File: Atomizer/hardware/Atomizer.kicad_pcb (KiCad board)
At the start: 2 copper layers, 54.6 x 98.6 mm, 41 parts

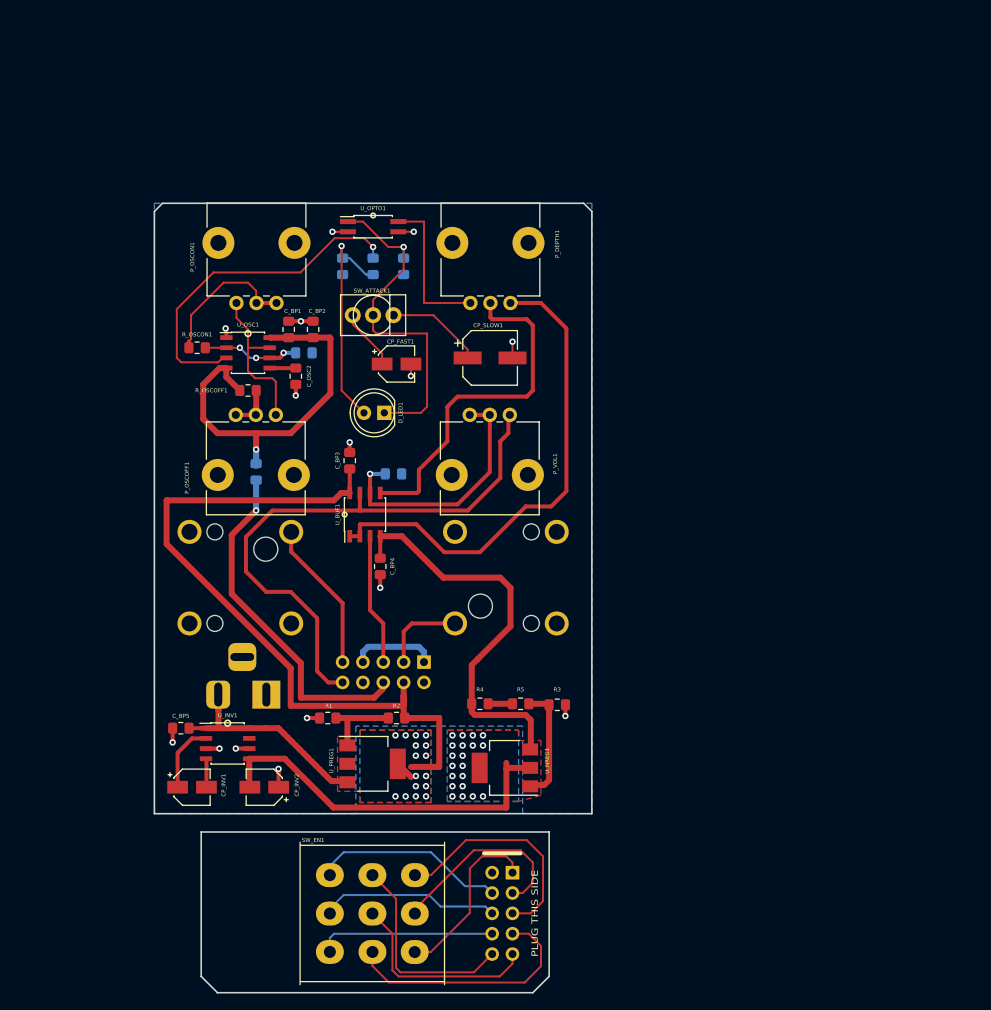
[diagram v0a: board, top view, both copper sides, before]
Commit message: Added 3d Model
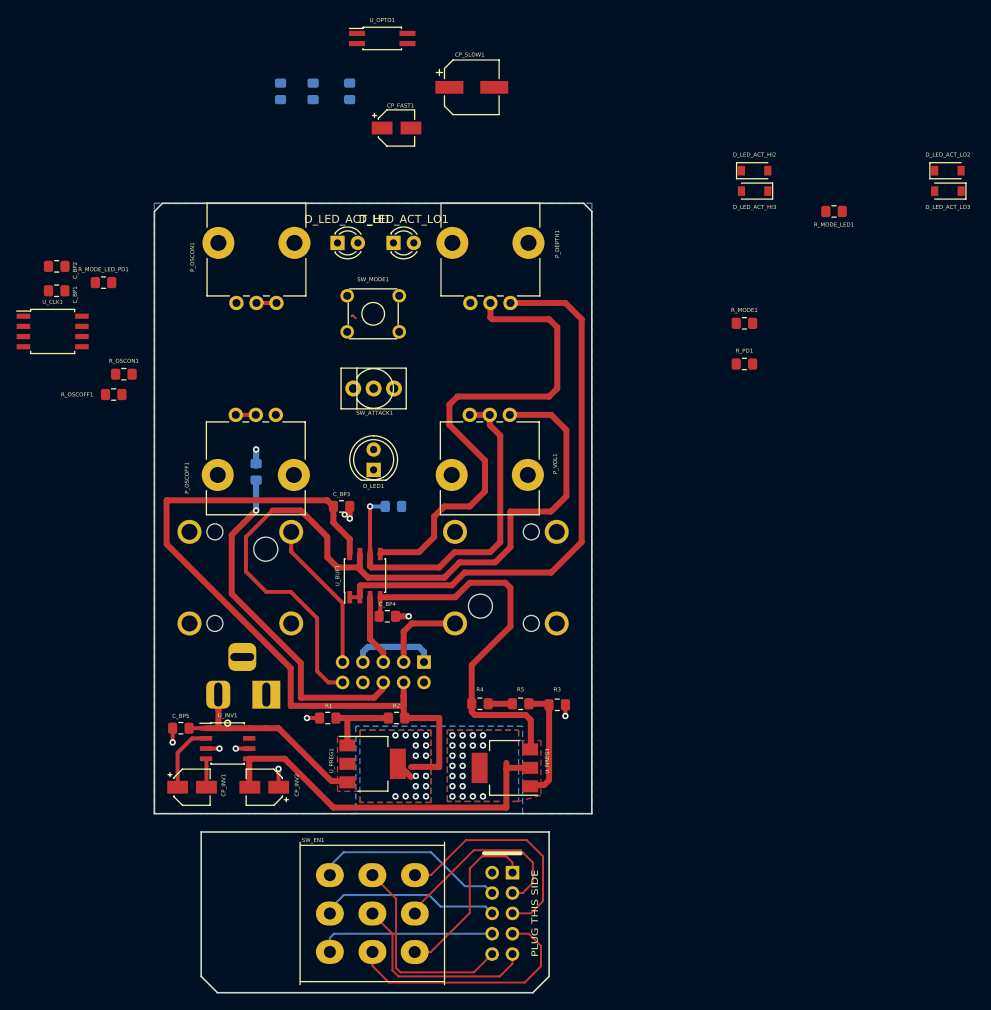
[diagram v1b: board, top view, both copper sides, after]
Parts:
- removed C_OSC1: 22uF, Capacitor_SMD:C_0805_2012Metric_Pad1.15x1.40mm_HandSolder
- removed C_OSC2: 100nF, Capacitor_SMD:C_0805_2012Metric_Pad1.15x1.40mm_HandSolder
- removed U_OSC1: TLC555, Package_SO:SOIC-8_3.9x4.9mm_P1.27mm
- added D_LED_ACT_HI1: LED, LED_THT:LED_D3.0mm, F.Cu at (76.2, 76.3)
- added D_LED_ACT_HI2: 1N914_VF1, Diode_SMD:D_SOD-123, F.Cu at (128.3, 67.3)
- added D_LED_ACT_HI3: 1N914_VF1, Diode_SMD:D_SOD-123, F.Cu at (128.3, 69.8)
- added D_LED_ACT_LO1: LED, LED_THT:LED_D3.0mm, F.Cu at (83.2, 76.3)
- added D_LED_ACT_LO2: 1N914_VF1, Diode_SMD:D_SOD-123, F.Cu at (152.4, 67.3)
- added D_LED_ACT_LO3: 1N914_VF1, Diode_SMD:D_SOD-123, F.Cu at (152.4, 69.8)
- added R_MODE1: 1K, Resistor_SMD:R_0805_2012Metric_Pad1.15x1.40mm_HandSolder, F.Cu at (127.0, 86.4)
- added R_MODE_LED1: 22K, Resistor_SMD:R_0805_2012Metric_Pad1.15x1.40mm_HandSolder, F.Cu at (138.2, 72.4)
- added R_MODE_LED_PD1: 47K, Resistor_SMD:R_0805_2012Metric_Pad1.15x1.40mm_HandSolder, F.Cu at (47.0, 81.3)
- added R_PD1: 22M, Resistor_SMD:R_0805_2012Metric_Pad1.15x1.40mm_HandSolder, F.Cu at (127.0, 91.4)
- added SW_MODE1: SW_SPST, TE_Alcoswitch_Tactile_FSM_RAJ:SW_TH_Tactile_Omron_B3F-10xx, F.Cu at (77.4, 82.9)
- added U_CLK1: ATtiny85-20SU, Package_SO:SOIJ-8_5.3x5.3mm_P1.27mm, F.Cu at (40.6, 87.4)
- C_BP2: value 47uF -> 10uF
- U_OPTO1: value LTV-357T -> ACPL-217
- moved CP_SLOW1 33.9 mm to (93.0, 56.9)
- moved C_BP2 33.0 mm to (41.1, 79.2), turned to 0 degrees
- moved CP_FAST1 29.5 mm to (83.6, 62.0)
- moved C_BP1 29.4 mm to (41.1, 82.3), turned to 0 degrees
- moved C_LPFOPT2 24.6 mm to (73.2, 57.4)
- moved U_OPTO1 23.5 mm to (81.8, 50.8)
- moved C_LPFOPT1 23.2 mm to (69.1, 57.4)
- moved R_LPF1 22.0 mm to (77.7, 57.4)
- moved R_OSCOFF1 16.8 mm to (48.3, 95.2)
- moved R_OSCON1 9.72 mm to (49.5, 92.7)
- moved SW_ATTACK1 9.15 mm to (80.7, 94.5), turned to 90 degrees
- moved U_BUF1 7.62 mm to (79.6, 117.9)
- moved D_LED1 7.24 mm to (80.7, 104.7), turned to 90 degrees
- moved C_BP4 6.29 mm to (82.4, 122.9), turned to 0 degrees
- moved C_BP3 5.80 mm to (76.7, 109.2), turned to 180 degrees
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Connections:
- net /555PWMTremolo_3PDT/3PDT_1_INT renamed /Atomizer_3PDT/3PDT_1_INT
- net /555PWMTremolo_3PDT/3PDT_2_INT renamed /Atomizer_3PDT/3PDT_2_INT
- net /555PWMTremolo_3PDT/3PDT_3_INT renamed /Atomizer_3PDT/3PDT_3_INT
- net /555PWMTremolo_3PDT/3PDT_4_INT renamed /Atomizer_3PDT/3PDT_4_INT
- net /555PWMTremolo_3PDT/3PDT_5_INT renamed /Atomizer_3PDT/3PDT_5_INT
- net /555PWMTremolo_3PDT/3PDT_6_INT renamed /Atomizer_3PDT/3PDT_6_INT
- net /555PWMTremolo_3PDT/3PDT_7_INT renamed /Atomizer_3PDT/3PDT_7_INT
- net /555PWMTremolo_3PDT/3PDT_8_INT renamed /Atomizer_3PDT/3PDT_8_INT
- net /555PWMTremolo_3PDT/3PDT_9_INT renamed /Atomizer_3PDT/3PDT_9_INT
- net /555PWMTremolo_Clock/CLK_OUT renamed /Atomizer_Clock/CLK_OUT
- P_OSCOFF1 pad 1: Net-(P_OSCOFF1-Pad1) -> /GND
- P_OSCOFF1 pad 2: Net-(P_OSCOFF1-Pad1) -> /Atomizer_Clock/FREQ_ADJ_OFF_PIN
- P_OSCON1 pad 1: Net-(P_OSCON1-Pad1) -> /GND
- P_OSCON1 pad 2: Net-(P_OSCON1-Pad1) -> /Atomizer_Clock/FREQ_ADJ_ON_PIN
- P_OSCON1 pad 3: Net-(P_OSCOFF1-Pad3) -> Net-(P_OSCON1-Pad3)
- R_LPF1 pad 2: Net-(R_LPF1-Pad2) -> /Atomizer_Clock/CLK_OUT_PIN
- R_OSCOFF1 pad 1: Net-(P_OSCOFF1-Pad1) -> Net-(P_OSCOFF1-Pad3)
- R_OSCOFF1 pad 2: Net-(C_BP1-Pad1) -> /3PDT_8_EXT
- R_OSCON1 pad 1: Net-(P_OSCON1-Pad1) -> Net-(P_OSCON1-Pad3)
- R_OSCON1 pad 2: Net-(C_OSC1-Pad1) -> /3PDT_8_EXT
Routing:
- net Net-(C_BP1-Pad1): track 50.3 -> 3.80 mm
- net Net-(C_LPFOPT2-Pad1): track 43.5 -> 0.00 mm, vias 1 -> 0
- net Net-(R_LPF1-Pad2): track 42.8 -> 0.00 mm, vias 1 -> 0
- net Net-(C_LPFOPT1-Pad1): track 28.2 -> 0.00 mm, vias 1 -> 0
- net /3PDT_6_EXT: track 72.0 -> 98.0 mm
- net Net-(P_OSCOFF1-Pad3): track 20.0 -> 0.00 mm
- net /Atomizer_Clock/CLK_OUT: track 19.2 -> 0.08 mm
- net Net-(P_DEPTH1-Pad2): track 44.1 -> 63.0 mm
- net Net-(P_OSCON1-Pad1): track 18.4 -> 2.56 mm
- net Net-(P_VOL1-Pad1): track 32.3 -> 46.3 mm
- net /GND: track 26.6 -> 13.9 mm, vias 15 -> 8
- net Net-(C_OSC1-Pad1): track 12.2 -> 0.00 mm, vias 3 -> 0
- net Net-(CP_SLOW1-Pad1): track 12.1 -> 0.00 mm
- net Net-(P_DEPTH1-Pad1): track 61.7 -> 70.1 mm
- net /3PDT_3_EXT: track 16.4 -> 8.78 mm
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
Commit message: Finished Atomizer RevB
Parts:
- removed C_LPFOPT1: 100nF, Capacitor_SMD:C_0805_2012Metric_Pad1.15x1.40mm_HandSolder
- removed C_LPFOPT2: 10uF, Capacitor_SMD:C_0805_2012Metric_Pad1.15x1.40mm_HandSolder
- removed R_MODE_LED_PD1: 47K, Resistor_SMD:R_0805_2012Metric_Pad1.15x1.40mm_HandSolder
- removed R_OSCLIMIT1: 330R, Resistor_SMD:R_0805_2012Metric_Pad1.15x1.40mm_HandSolder
- added J_ICSP1: Conn_02x03_Odd_Even, Connector_PinHeader_2.54mm:PinHeader_2x03_P2.54mm_Vertical, B.Cu at (57.3, 90.3)
- moved D_LED_ACT_LO3 75.0 mm to (77.5, 72.7)
- moved D_LED_ACT_LO2 68.5 mm to (84.2, 72.7), turned to 180 degrees
- moved R_MODE_LED1 65.1 mm to (74.3, 85.1), turned to 270 degrees
- moved R_PD1 58.4 mm to (78.5, 123.9), turned to 270 degrees
- moved R_MODE1 52.9 mm to (74.3, 90.8), turned to 90 degrees
- moved D_LED_ACT_HI2 52.7 mm to (77.5, 81.3), turned to 180 degrees
- moved R_LPF1 49.9 mm to (76.2, 107.3)
- moved D_LED_ACT_HI3 45.2 mm to (84.6, 81.3)
- moved CP_SLOW1 35.1 mm to (101.3, 90.9)
- moved U_OPTO1 34.4 mm to (84.7, 85.1)
- moved CP_FAST1 30.3 mm to (92.8, 90.9)
- moved U_CLK1 26.8 mm to (67.3, 90.2), turned to 180 degrees
- moved C_BP2 24.7 mm to (61.0, 94.0), turned to 180 degrees
- moved C_BP1 24.0 mm to (61.0, 95.9), turned to 180 degrees
- moved R_OSCON1 16.3 mm to (56.8, 78.1), turned to 90 degrees
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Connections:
- C_BP1 pad 1: Net-(C_BP1-Pad1) -> /3PDT_8_EXT
- C_BP2 pad 1: Net-(C_BP1-Pad1) -> /3PDT_8_EXT
- U_CLK1 pad 1: (no net) -> /Atomizer_Clock/RESET
- U_CLK1 pad 8: Net-(C_BP1-Pad1) -> /3PDT_8_EXT
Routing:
- net /3PDT_8_EXT: track 42.8 -> 124.7 mm, vias 1 -> 0
- net /Atomizer_Clock/MODE_LED_PIN: track 0.00 -> 40.9 mm, vias 0 -> 2
- net /Atomizer_Clock/CLK_OUT_PIN: track 0.00 -> 30.6 mm, vias 0 -> 2
- net Net-(CP_SLOW1-Pad1): track 0.00 -> 26.9 mm
- net Net-(D_LED1-Pad1): track 0.00 -> 23.9 mm
- net Net-(CP_FAST1-Pad1): track 0.72 -> 22.7 mm, vias 0 -> 2
- net /Atomizer_Clock/RESET: track 0.00 -> 19.7 mm
- net /Atomizer_Clock/MODE_BTN_PIN: track 0.00 -> 17.9 mm
- net Net-(P_OSCOFF1-Pad3): track 0.00 -> 15.4 mm
- net Net-(D_LED_ACT_HI1-Pad2): track 0.00 -> 15.0 mm
- net /GND: track 13.9 -> 28.8 mm, vias 8 -> 17
- net +5V: track 98.9 -> 85.8 mm, vias 16 -> 18
- net /Atomizer_Clock/FREQ_ADJ_OFF_PIN: track 0.00 -> 11.5 mm, vias 0 -> 1
- net /Atomizer_Clock/FREQ_ADJ_ON_PIN: track 0.00 -> 9.84 mm
- net Net-(P_OSCON1-Pad3): track 0.00 -> 9.79 mm
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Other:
- board text removed: "Jumper if not req’d"
- board text removed: "higher val lower range"

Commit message: Finished Atomizer RevB
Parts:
- added D_LED_ACT_HI4: 1N914_VF1, Diode_SMD:D_SOD-123, F.Cu at (104.6, 79.4)
- added D_LED_ACT_LO4: 1N914_VF1, Diode_SMD:D_SOD-123, F.Cu at (56.9, 75.7)
- R_LPF1: value 100R -> 1K
- moved R_OSCON1 2.54 mm to (56.9, 80.6)
- moved D_LED_ACT_HI3 0.51 mm to (85.1, 81.3)
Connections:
- D_LED_ACT_HI3 pad 1: /GND -> Net-(D_LED_ACT_HI3-Pad1)
- D_LED_ACT_LO3 pad 2: /3PDT_8_EXT -> Net-(D_LED_ACT_LO3-Pad2)
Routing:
- net /3PDT_8_EXT: track 124.7 -> 101.5 mm
- net Net-(D_LED_ACT_LO3-Pad2): track 0.00 -> 19.6 mm
- net Net-(D_LED_ACT_HI3-Pad1): track 0.00 -> 18.0 mm
- net Net-(P_OSCON1-Pad3): track 9.79 -> 7.57 mm

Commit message: Finished Atomizer RevA
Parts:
- removed D_LED_ACT_HI1, D_LED_ACT_LO1: LED, LED_THT:LED_D3.0mm
- removed D_LED_ACT_HI2, D_LED_ACT_HI3, D_LED_ACT_HI4, D_LED_ACT_LO2, D_LED_ACT_LO3, D_LED_ACT_LO4: 1N914_VF1, Diode_SMD:D_SOD-123
- removed R_MODE_LED1: 22K, Resistor_SMD:R_0805_2012Metric_Pad1.15x1.40mm_HandSolder
- added D_HI1: 1N914_VF1, Diode_SMD:D_SOD-123, F.Cu at (77.5, 81.3)
- added D_HI2: 1N914_VF1, Diode_SMD:D_SOD-123, F.Cu at (85.1, 81.3)
- added D_HI3: 1N914_VF1, Diode_SMD:D_SOD-123, F.Cu at (104.6, 79.6)
- added D_LEDHI1: LED, LED_THT:LED_D3.0mm, F.Cu at (75.8, 77.2)
- added D_LEDLO1: LED, LED_THT:LED_D3.0mm, F.Cu at (83.3, 77.2)
- added D_LO1: 1N914_VF1, Diode_SMD:D_SOD-123, F.Cu at (84.1, 72.8)
- added D_LO2: 1N914_VF1, Diode_SMD:D_SOD-123, F.Cu at (77.5, 72.8)
- added D_LO3: 1N914_VF1, Diode_SMD:D_SOD-123, F.Cu at (56.9, 75.7)
- added R_MLED1: 22K, Resistor_SMD:R_0805_2012Metric_Pad1.15x1.40mm_HandSolder, F.Cu at (77.5, 85.1)
- J_IN1, J_OUT1: footprint custom_sockets:6_35MM_JACK_MONO_FlatTop -> custom_sockets:6_35MM_JACK_MONO_FlatTop_notab
- SW_MODE1: value SW_SPST -> 1-1825910-4; footprint TE_Alcoswitch_Tactile_FSM_RAJ:SW_TH_Tactile_Omron_B3F-10xx -> TE_Alcoswitch_Tactile_1-1825910-4:TE_1-1825910-4
- moved C_BP3 32.1 mm to (96.9, 135.6)
- moved R_PD1 26.3 mm to (104.1, 129.5), turned to 0 degrees
- moved C_BP4 25.6 mm to (104.1, 136.5), turned to 0 degrees
- moved U_BUF1 22.8 mm to (98.4, 130.8), turned to 180 degrees
- moved R_GAIN1 18.8 mm to (98.2, 101.2)
- moved R4 11.4 mm to (104.1, 139.1)
- moved R3 10.2 mm to (104.1, 144.1)
- moved R5 9.26 mm to (104.1, 141.6), turned to 180 degrees
- moved SW_MODE1 3.98 mm to (80.7, 90.9), turned to 180 degrees
- moved U_OPTO1 1.02 mm to (85.7, 85.1)
- moved R1 0.25 mm to (75.0, 135.9)
- moved R2 0.25 mm to (83.6, 135.9)
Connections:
- SW_MODE1 pad 1: Net-(R_MODE1-Pad2) -> (no net)
- SW_MODE1 pad 2: /GND -> Net-(R_MODE1-Pad2)
- SW_MODE1 pad 3: (no net) -> /GND
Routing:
- net +5V: track 85.8 -> 34.7 mm, vias 18 -> 16
- net /3PDT_3_EXT: track 10.6 -> 38.5 mm, vias 0 -> 2
- net -5V: track 46.5 -> 18.6 mm
- net Net-(D_LED_ACT_LO3-Pad2): track 19.6 -> 0.00 mm
- net Net-(D_LO2-Pad2): track 0.00 -> 19.5 mm
- net Net-(D_LED_ACT_HI3-Pad1): track 18.0 -> 0.00 mm
- net Net-(D_HI2-Pad1): track 0.00 -> 18.0 mm
- net Net-(D_LED_ACT_HI1-Pad2): track 15.0 -> 0.00 mm
- net /3PDT_6_EXT: track 96.3 -> 111.3 mm, vias 0 -> 2
- net Net-(D_LEDHI1-Pad2): track 0.00 -> 13.6 mm
- net Net-(P_DEPTH1-Pad1): track 70.2 -> 61.1 mm
- net Net-(R3-Pad1): track 14.7 -> 5.76 mm
- net /Atomizer_Clock/MODE_LED_PIN: track 40.9 -> 35.4 mm
- net Net-(D_HI1-Pad2): track 0.00 -> 4.60 mm
- net Net-(D_LED_ACT_LO1-Pad2): track 4.47 -> 0.00 mm
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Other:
- board text added: "ATOMIZER Chris Sutton 2018 RevA"
- board text added: "ATOMIZER Chris Sutton RevA 2018"
- board text added: "Max 1K"
- board text removed: "OPTO TREM Chris Sutton 2018 RevB"
- board text removed: "OPTO TREM Chris Sutton RevB 2018"

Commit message: Updated BOM
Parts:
- SW_MODE1: footprint TE_Alcoswitch_Tactile_1-1825910-4:TE_1-1825910-4 -> TE_Alcoswitch_Tactile_2-1825910-7:SW_2-1825910-7
- turned SW_MODE1 to 0 degrees
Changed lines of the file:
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@@
   )
   (setup
-    (last_trace_width 0.5)
+    (last_trace_width 0.25)
     (user_trace_width 0.5)
     (user_trace_width 0.75)
@@
     (add_net "Net-(R_MODE1-Pad2)")
   )
+  (module TE_Alcoswitch_Tactile_2-1825910-7:SW_2-1825910-7 (layer F.Cu)
+    (at 80.7085 90.8685)
+    (fp_text reference SW_MODE1 (at -2.98289 -3.90753) (layer F.SilkS)
+      (effects (font (size 0.480336 0.480336) (thickness 0.05)))
+    )
+    (fp_text value 1-1825910-4 (at -2.67975 3.70038) (layer F.SilkS)
+      (effects (font (size 0.480673 0.480673) (thickness 0.05)))
+    )
+    (fp_circle (center -4.778 -2.132) (end -4.678 -2.132) (layer F.SilkS) (width 0.3))
+    (fp_circle (center -2.379 -2.3) (end -2.279 -2.3) (layer Dwgs.User) (width 0.3))
+    (fp_line (start 4.25 3.25) (end -4.25 3.25) (layer Eco1.User) (width 0.05))
+    (fp_line (start 4.25 -3.25) (end 4.25 3.25) (layer Eco1.User) (width 0.05))
+    (fp_line (start -4.25 -3.25) (end 4.25 -3.25) (layer Eco1.User) (width 0.05))
+    (fp_line (start -4.25 3.25) (end -4.25 -3.25) (layer Eco1.User) (width 0.05))
+    (fp_line (start -2.4 3) (end 2.4 3) (layer F.SilkS) (width 0.127))
+    (fp_line (start 2.995 -1.15) (end 2.995 1.15) (layer F.SilkS) (width 0.127))
+    (fp_line (start -2.13 -2.995) (end 2.37 -2.995) (layer F.SilkS) (width 0.127))
+    (fp_line (start -2.995 -1.12) (end -2.995 1.15) (layer F.SilkS) (width 0.127))
+    (fp_line (start 2.995 2.995) (end -2.995 2.995) (layer Dwgs.User) (width 0.127))
+    (fp_line (start 2.995 -2.995) (end 2.995 2.995) (layer Dwgs.User) (width 0.127))
+    (fp_line (start -2.995 -2.995) (end 2.995 -2.995) (layer Dwgs.User) (width 0.127))
+    (fp_line (start -2.995 2.995) (end -2.995 -2.995) (layer Dwgs.User) (width 0.127))
+    (pad 3 thru_hole circle (at 3.25 -2.25) (size 1.498 1.498) (drill 0.99) (layers *.Cu *.Mask)
+      (net 20 /GND))
+    (pad 4 thru_hole circle (at 3.25 2.25) (size 1.498 1.498) (drill 0.99) (layers *.Cu *.Mask))
+    (pad 2 thru_hole circle (at -3.25 2.25) (size 1.498 1.498) (drill 0.99) (layers *.Cu *.Mask)
+      (net 38 "Net-(R_MODE1-Pad2)"))
+    (pad 1 thru_hole rect (at -3.25 -2.25) (size 1.498 1.498) (drill 0.99) (layers *.Cu *.Mask))
+    (model ${KIPRJMOD}/LIBS/3D/c-2-1825910-7-c-3d.stp
+      (offset (xyz 0 0 13))
+      (scale (xyz 1 1 1))
+      (rotate (xyz 0 0 -90))
+    )
+  )
   (module custom_sockets:6_35MM_JACK_MONO_FlatTop_notab (layer B.Cu)
     (at 97.028 118.11)
@@
       (scale (xyz 1 1 1))
       (rotate (xyz 0 0 0))
-    )
-  )
-  (module TE_Alcoswitch_Tactile_1-1825910-4:TE_1-1825910-4 (layer F.Cu)
-    (at 80.7085 90.8685 180)
-    (fp_text reference SW_MODE1 (at 0.1905 -3.556 180) (layer F.SilkS)
-      (effects (font (size 0.5 0.5) (thickness 0.125)))
-    )
-    (fp_text value 1-1825910-4 (at 0.6985 -3.7465 180) (layer F.SilkS) hide
-      (effects (font (size 0.5 0.5) (thickness 0.125)))
-    )
-    (fp_line (start -2.995 -2.995) (end -2.995 2.995) (layer Dwgs.User) (width 0.127))
-    (fp_line (start -2.995 2.995) (end 2.995 2.995) (layer Dwgs.User) (width 0.127))
-    (fp_line (start 2.995 2.995) (end 2.995 -2.995) (layer Dwgs.User) (width 0.127))
-    (fp_line (start 2.995 -2.995) (end -2.995 -2.995) (layer Dwgs.User) (width 0.127))
-    (fp_line (start -2 -3) (end 2 -3) (layer F.SilkS) (width 0.127))
-    (fp_line (start 3 -1) (end 3 1) (layer F.SilkS) (width 0.127))
-    (fp_line (start -3 -1) (end -3 1) (layer F.SilkS) (width 0.127))
-    (fp_line (start -2 3) (end 2 3) (layer F.SilkS) (width 0.127))
-    (fp_circle (center 0 0) (end 1.11803 0) (layer F.SilkS) (width 0.127))
-    (fp_circle (center 0 0) (end 1.11803 0) (layer Dwgs.User) (width 0.127))
-    (fp_circle (center -4.733 -2.2711) (end -4.633 -2.2711) (layer F.SilkS) (width 0.2))
-    (fp_line (start -4.25 -3.25) (end -4.25 3.25) (layer Eco1.User) (width 0.05))
-    (fp_line (start -4.25 3.25) (end 4.25 3.25) (layer Eco1.User) (width 0.05))
-    (fp_line (start 4.25 3.25) (end 4.25 -3.25) (layer Eco1.User) (width 0.05))
-    (fp_line (start 4.25 -3.25) (end -4.25 -3.25) (layer Eco1.User) (width 0.05))
-    (pad 1 thru_hole rect (at -3.25 -2.25 180) (size 1.498 1.498) (drill 0.99) (layers *.Cu *.Mask))
-    (pad 3 thru_hole circle (at -3.25 2.25 180) (size 1.498 1.498) (drill 0.99) (layers *.Cu *.Mask)
-      (net 20 /GND))
-    (pad 2 thru_hole circle (at 3.25 -2.25 180) (size 1.498 1.498) (drill 0.99) (layers *.Cu *.Mask)
-      (net 38 "Net-(R_MODE1-Pad2)"))
-    (pad 4 thru_hole circle (at 3.25 2.25 180) (size 1.498 1.498) (drill 0.99) (layers *.Cu *.Mask))
-    (model ${KIPRJMOD}/LIBS/3D/c-2-1825910-7-c-3d.stp
-      (offset (xyz 0 0 13.25))
-      (scale (xyz 1 1 1))
-      (rotate (xyz 0 0 90))
     )
   )
@@
   (segment (start 86.36 96.774) (end 86.36 90.7415) (width 0.5) (layer F.Cu) (net 22))
   (segment (start 83.312 99.822) (end 86.36 96.774) (width 0.5) (layer F.Cu) (net 22))
-  (segment (start 75.82 76.834) (end 76.2 76.454) (width 0.75) (layer F.Cu) (net 43) (status 30))
-  (segment (start 83.185 81.28) (end 79.12 81.28) (width 0.75) (layer F.Cu) (net 44) (status 30))
-  (segment (start 85.852 72.8218) (end 85.8012 72.771) (width 0.75) (layer F.Cu) (net 47) (status 30))
-  (segment (start 85.852 77.216) (end 85.852 72.8218) (width 0.75) (layer F.Cu) (net 47) (status 30))
-  (segment (start 79.0809 72.7202) (end 82.3849 72.7202) (width 0.75) (layer F.Cu) (net 48) (status 30))
   (segment (start 75.2475 154.1145) (end 75.2475 155.2448) (width 0.25) (layer B.Cu) (net 23) (status 30))
   (segment (start 76.962 152.4) (end 75.2475 154.1145) (width 0.25) (layer B.Cu) (net 23) (status 20))
@@
   (segment (start 80.699741 108.467) (end 80.708741 108.458) (width 0.75) (layer B.Cu) (net 42) (status 30))
   (segment (start 76.2 108.467) (end 80.699741 108.467) (width 0.75) (layer B.Cu) (net 42) (status 30))
+  (segment (start 75.82 76.834) (end 76.2 76.454) (width 0.75) (layer F.Cu) (net 43) (status 30))
   (segment (start 75.82 77.217) (end 75.819 77.216) (width 0.75) (layer F.Cu) (net 43))
   (segment (start 75.82 81.28) (end 75.82 77.217) (width 0.75) (layer F.Cu) (net 43))
+  (segment (start 83.185 81.28) (end 79.12 81.28) (width 0.75) (layer F.Cu) (net 44) (status 30))
   (segment (start 104.393 81.28) (end 104.648 81.025) (width 0.75) (layer F.Cu) (net 45) (status 30))
   (segment (start 86.74 81.28) (end 104.393 81.28) (width 0.75) (layer F.Cu) (net 45) (status 30))
@@
   (segment (start 76.445 85.09) (end 76.445 83.575) (width 0.5) (layer F.Cu) (net 46))
   (segment (start 78.359 77.216) (end 83.312 77.216) (width 0.75) (layer F.Cu) (net 46))
+  (segment (start 85.852 72.8218) (end 85.8012 72.771) (width 0.75) (layer F.Cu) (net 47) (status 30))
+  (segment (start 85.852 77.216) (end 85.852 72.8218) (width 0.75) (layer F.Cu) (net 47) (status 30))
+  (segment (start 79.0809 72.7202) (end 82.3849 72.7202) (width 0.75) (layer F.Cu) (net 48) (status 30))
   (segment (start 74.8827 72.7075) (end 75.8327 72.7075) (width 0.5) (layer F.Cu) (net 49) (status 20))
   (segment (start 57.046 74.042) (end 58.3805 72.7075) (width 0.5) (layer F.Cu) (net 49) (status 10))
